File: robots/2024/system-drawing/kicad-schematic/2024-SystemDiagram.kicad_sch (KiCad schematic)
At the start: 207 parts

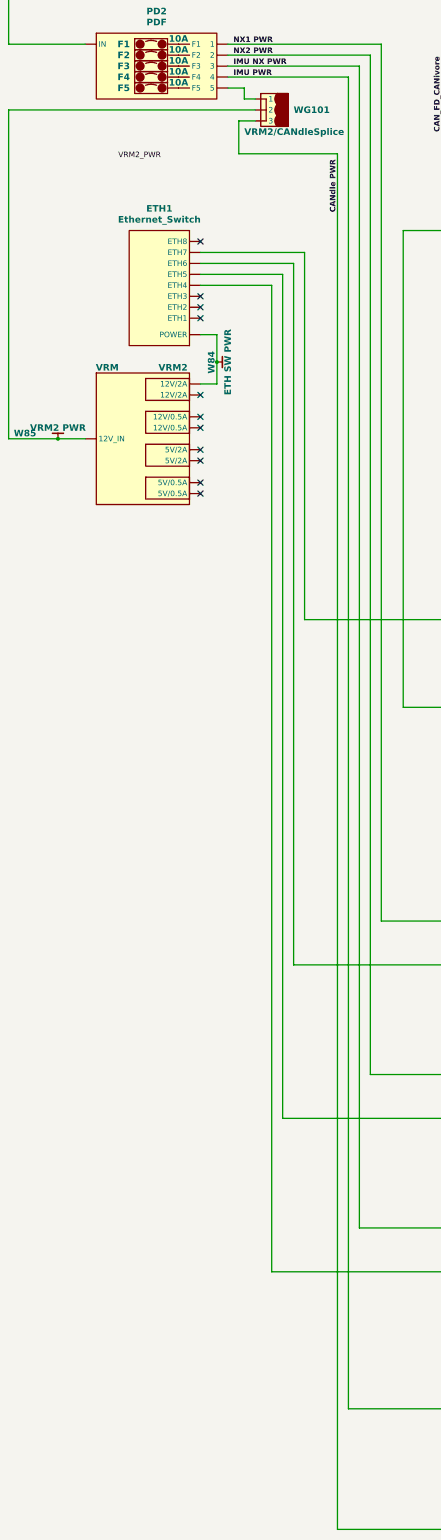
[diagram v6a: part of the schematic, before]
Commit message: Move Candle to VRM2 in sys dwg
Signed-off-by: Scott Berman <sgberman1@gmail.com>
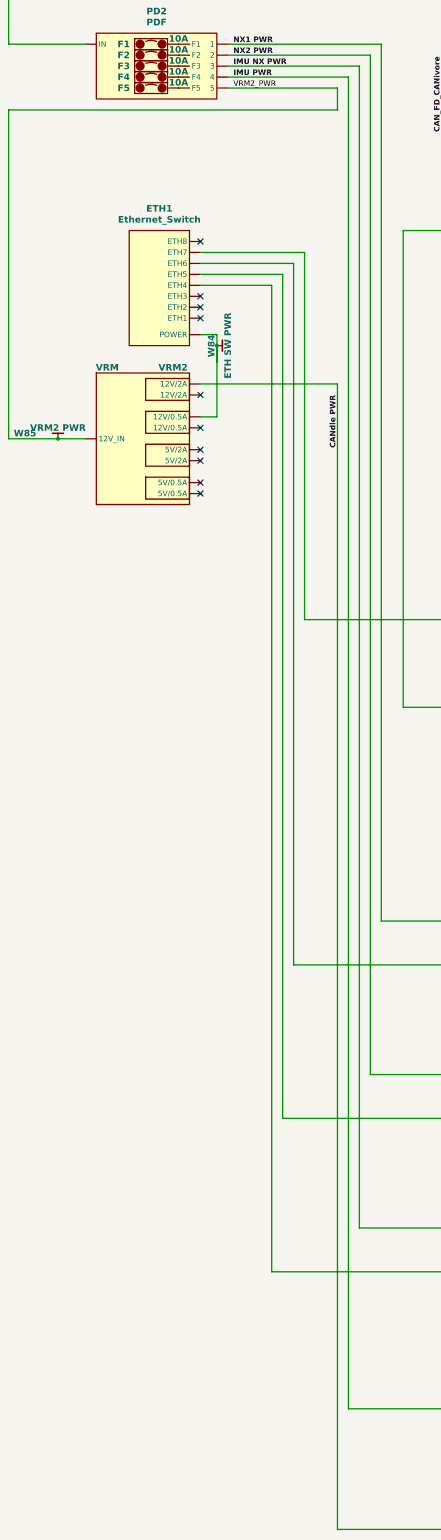
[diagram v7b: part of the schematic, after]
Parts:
- removed WG101: VRM2/CANdleSplice, symbol SystemDiagram:Wago_3
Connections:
- net CANdle PWR: now also VRM2. (5V/2A)
- net VRM2_PWR: now also PD2. (IN), VRM2. (5V/2A), W85.
- net at POE1. (RJ45S): now also RDO1. (POWER); no longer VRM1. (5V/2A)
- net at RDO1. (POWER): now also ETH1. (POWER); no longer VRM1. (5V/2A)
- net at ETH1. (POWER): now also NX1. (Power), W87.; no longer RDO1. (POWER)
- new net: VRM1. (5V/2A), W118., WG1. (4)
- new net: POE1. (RJ45S), VRM1. (5V/2A)
- new net: RDO1. (POWER), VRM1. (5V/2A)
- new net: CAN1. (USB), W67., WG1. (4)
- new net: ETH1. (POWER), NX2. (Power), W88.
- new net: MOT10. (PWR), MOT12. (PWR), W111.
- new net: ETH1. (POWER), VRM2. (5V/2A), W84.
- new net: ETH1. (POWER), NX3. (Power), W89.
- new net: MOT1. (PWR), MOT2. (PWR), W105.
- new net: MOT3. (PWR), MOT4. (PWR), W107.
- new net: IMU1. (RIO_PWM2), NX3. (Power), W47.
- no-connect marks 73 -> 72
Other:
- moved on the sheet: W84
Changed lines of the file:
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@@
   (junction (at 171.45 426.72) (diameter 0) (color 0 0 0 0)
   )
-  (junction (at 91.44 251.46) (diameter 0) (color 0 0 0 0)
-  )
   (junction (at 582.93 474.98) (diameter 0) (color 0 0 0 0)
   )
@@
   (junction (at 281.94 492.76) (diameter 0) (color 0 0 0 0)
   )
+  (junction (at 91.44 247.65) (diameter 0) (color 0 0 0 0)
+  )
   (junction (at 237.49 232.41) (diameter 0) (color 0 0 0 0)
   )
@@
   (no_connect (at 224.79 426.72))
   (no_connect (at 87.63 236.22))
-  (no_connect (at 87.63 264.16))
   (no_connect (at 220.98 259.08))
   (no_connect (at 191.77 469.9))
@@
     (stroke (width 0.254) (type default) (color 255 0 0 1))
   )
+  (wire (pts (xy 87.63 256.54) (xy 119.38 256.54))
+    (stroke (width 0.508) (type default) (color 255 0 0 1))
+  )
   (wire (pts (xy 487.68 326.39) (xy 436.88 326.39))
     (stroke (width 0.508) (type default) (color 255 0 0 1))
@@
     (stroke (width 0.254) (type default) (color 255 153 0 1))
   )
-  (wire (pts (xy 93.98 187.96) (xy 97.79 187.96))
-    (stroke (width 0.508) (type default) (color 255 0 0 1))
-  )
-  (wire (pts (xy 96.52 203.2) (xy 96.52 195.58))
+  (wire (pts (xy 93.98 187.96) (xy 119.38 187.96))
     (stroke (width 0.508) (type default) (color 255 0 0 1))
   )
@@
     (stroke (width 0.508) (type default) (color 255 0 0 1))
   )
-  (wire (pts (xy 96.52 195.58) (xy 100.33 195.58))
-    (stroke (width 0.508) (type default) (color 255 0 0 1))
-  )
-  (wire (pts (xy 87.63 256.54) (xy 91.44 256.54))
-    (stroke (width 0.254) (type default) (color 255 0 0 1))
-  )
   (wire (pts (xy 165.1 149.86) (xy 165.1 205.74))
     (stroke (width 0.508) (type default) (color 255 0 0 1))
@@
     (stroke (width 0.508) (type default) (color 255 0 0 1))
   )
-  (wire (pts (xy 91.44 245.11) (xy 91.44 251.46))
+  (wire (pts (xy 91.44 245.11) (xy 91.44 247.65))
     (stroke (width 0.254) (type default) (color 255 0 0 1))
   )
@@
     (stroke (width 0.508) (type default) (color 255 0 0 1))
   )
-  (wire (pts (xy 97.79 190.5) (xy 100.33 190.5))
-    (stroke (width 0.508) (type default) (color 255 0 0 1))
-  )
   (wire (pts (xy 73.025 64.77) (xy 92.71 64.77))
     (stroke (width 0.508) (type default) (color 255 0 0 1))
@@
     (stroke (width 0.508) (type default) (color 255 0 0 1))
   )
-  (wire (pts (xy 119.38 203.2) (xy 96.52 203.2))
-    (stroke (width 0.508) (type default) (color 255 0 0 1))
-  )
   (wire (pts (xy 580.39 400.05) (xy 595.63 400.05))
     (stroke (width 0) (type default))
@@
     (stroke (width 0.508) (type default) (color 255 0 0 1))
   )
-  (wire (pts (xy 119.38 203.2) (xy 119.38 521.97))
-    (stroke (width 0.508) (type default) (color 255 0 0 1))
-  )
   (wire (pts (xy 487.68 341.63) (xy 552.45 341.63))
     (stroke (width 0.254) (type default) (color 194 0 194 1))
@@
     (stroke (width 0.508) (type default) (color 255 0 0 1))
   )
+  (wire (pts (xy 91.44 247.65) (xy 91.44 251.46))
+    (stroke (width 0) (type default))
+  )
   (wire (pts (xy 601.98 331.47) (xy 607.06 331.47))
     (stroke (width 0.254) (type default) (color 255 153 0 1))
@@
     (stroke (width 0.254) (type default) (color 194 0 194 1))
   )
-  (wire (pts (xy 97.79 187.96) (xy 97.79 190.5))
+  (wire (pts (xy 119.38 187.96) (xy 119.38 193.04))
     (stroke (width 0.508) (type default) (color 255 0 0 1))
   )
@@
     (stroke (width 0.254) (type default) (color 255 153 0 1))
   )
+  (wire (pts (xy 91.44 264.16) (xy 87.63 264.16))
+    (stroke (width 0.254) (type default) (color 255 0 0 1))
+  )
   (wire (pts (xy 401.32 194.31) (xy 401.32 368.3))
     (stroke (width 0.254) (type default) (color 194 0 194 1))
   )
-  (wire (pts (xy 91.44 251.46) (xy 91.44 256.54))
+  (wire (pts (xy 91.44 247.65) (xy 91.44 264.16))
     (stroke (width 0.254) (type default) (color 255 0 0 1))
   )
@@
     (stroke (width 0.508) (type default) (color 255 0 0 1))
   )
+  (wire (pts (xy 119.38 256.54) (xy 119.38 521.97))
+    (stroke (width 0.508) (type default) (color 255 0 0 1))
+  )
   (wire (pts (xy 534.67 144.78) (xy 510.54 144.78))
     (stroke (width 0.254) (type default) (color 194 0 194 1))
@@
     (stroke (width 0.254) (type default) (color 194 0 194 1))
   )
-  (wire (pts (xy 43.18 193.04) (xy 100.33 193.04))
+  (wire (pts (xy 43.18 193.04) (xy 119.38 193.04))
     (stroke (width 0.508) (type default) (color 255 0 0 1))
   )
@@
     (effects (font (face "FreeSans") (size 1.27 1.27) bold) (justify left bottom))
   )
-  (label "CANdle PWR" (at 119.38 204.47 270) (fields_autoplaced)
+  (label "CANdle PWR" (at 119.38 259.08 270) (fields_autoplaced)
     (effects (font (face "FreeSans") (size 1.27 1.27) bold) (justify right bottom))
   )
-  (label "VRM2_PWR" (at 68.58 204.47 0) (fields_autoplaced)
-    (effects (font (size 1.27 1.27)) (justify left bottom))
-  )
   (label "CAN_CLIMBER_TO_INTAKE" (at 591.82 391.16 180) (fields_autoplaced)
     (effects (font (face "FreeSans") (size 1.27 1.27) (thickness 0.254) bold) (justify right bottom))
@@
     (effects (font (face "FreeSans") (size 1.27 1.27) bold) (justify right bottom))
   )
+  (label "VRM2_PWR" (at 95.25 187.96 0) (fields_autoplaced)
+    (effects (font (size 1.27 1.27)) (justify left bottom))
+  )
   (label "DUMP BB PWR" (at 529.59 439.42 180) (fields_autoplaced)
     (effects (font (face "FreeSans") (size 1.27 1.27) bold) (justify right bottom))
@@
     )
   )
-  (symbol (lib_id "SystemDiagram:WireTag") (at 91.44 251.46 270) (unit 1)
+  (symbol (lib_id "SystemDiagram:WireTag") (at 91.44 247.65 270) (unit 1)
     (in_bom yes) (on_board yes) (dnp no)
-    (property "Reference" "W84" (at 90.17 248.92 0)
+    (property "Reference" "W84" (at 90.17 245.11 0)
       (effects (font (face "FreeSans") (size 1.524 1.524) bold) (justify left))
     )
-    (property "Value" "ETH SW PWR" (at 93.98 251.46 0)
+    (property "Value" "ETH SW PWR" (at 93.98 247.65 0)
       (effects (font (face "FreeSans") (size 1.524 1.524) bold))
     )
-    (property "Footprint" "" (at 91.44 251.46 0)
+    (property "Footprint" "" (at 91.44 247.65 0)
       (effects (font (size 1.27 1.27)) hide)
     )
-    (property "Datasheet" "" (at 91.44 251.46 0)
+    (property "Datasheet" "" (at 91.44 247.65 0)
       (effects (font (size 1.27 1.27)) hide)
     )
@@
         )
       )
-    )
-  )
-  (symbol (lib_id "SystemDiagram:Wago_3") (at 102.87 193.04 0) (unit 1)
-    (in_bom yes) (on_board yes) (dnp no)
-    (property "Reference" "WG101" (at 109.22 193.04 0)
-      (effects (font (face "FreeSans") (size 1.524 1.524) bold) (justify left))
-    )
-    (property "Value" "VRM2/CANdleSplice" (at 97.79 198.12 0)
-      (effects (font (face "FreeSans") (size 1.524 1.524) bold) (justify left))
-    )
-    (property "Footprint" "" (at 102.87 193.04 0)
-      (effects (font (size 1.27 1.27)) hide)
-    )
-    (property "Datasheet" "" (at 102.87 193.04 0)
-      (effects (font (size 1.27 1.27)) hide)
-    )
-    (pin "")
-    (pin "")
-    (pin "")
-    (instances
-      (project "2024-SystemDiagram"
-        (path "/12a52703-e3f4-4774-b510-3055ab1abf35"
-          (reference "WG101") (unit 1)
-        )
-      )

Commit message: Sys dwg: Swap right and left robot, move alt and catapult motors to FD
Signed-off-by: Scott Berman <sgberman1@gmail.com>
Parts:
- removed CAN4: CAN_Terminator, symbol SystemDiagram:CAN_Terminator
- removed W51: CATAPULT2 PWM, symbol SystemDiagram:WireTag
- removed WJ104: ~, symbol SystemDiagram:Wire_Junction
- added CAN102: CAN_Terminator, symbol SystemDiagram:CAN_Terminator
- added W133: CAN, symbol SystemDiagram:WireTag
- ENC1: value Left Shaft_Encoder -> Right Shaft_Encoder
- ENC2: value Right Shaft_Encoder -> Left Shaft_Encoder
- MOT1: value Kraken Left Front Drive Motor -> Kraken Right Back Drive Motor; CAN ID FD ID 4 -> FD ID 1
- MOT2: value Kraken Left Back Drive Motor -> Kraken Right Front Drive Motor; CAN ID FD ID 5 -> FD ID 2
- MOT3: value Kraken Right Front Drive Motor -> Kraken Left Back Drive Motor; CAN ID FD ID 2 -> FD ID 5
- MOT4: value Kraken Right Back Drive Motor -> Kraken Left Front Drive Motor; CAN ID FD ID 1 -> FD ID 4
- MOT5: CAN ID (none) -> FD ID 14
- MOT6: CAN ID (none) -> FD ID 15
- MOT7: CAN ID CAN ID 9 -> FD ID 9
- NX1: value NX1 -> NX1-LEFT
- NX2: value NX2 -> NX2-RIGHT
- W122: value CATAPULT1 PWM -> CAN
- W124: value CATAPULT2 PWM -> CAN
- W22: value Left Shaft Encoder -> Right Shaft Encoder
- W23: value Right Shaft Encoder -> Left Shaft Encoder
- W4: value LEFT FRONT DRIVE PWR -> RIGHT BACK DRIVE PWR
- W5: value LEFT BACK DRIVE PWR -> RIHGT FRONT DRIVE PWR
- W6: value RIGHT FRONT DRIVE PWR -> LEFT_BACK_DRIVE PWR
- W7: value RIGHT BACK DRIVE PWR -> LEFT FRONT DRIVE PWR
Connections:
- net CLIMBER ENC POT RIO: now also RIO1.ENC_AD4; no longer RIO1.ENC_AD5
- net LEFT BACK DRIVE PWR: now also MOT3. (PWR), PD1.T14, W6.; no longer MOT2. (PWR), PD1.T1, W5.
- net LEFT ENC: now also ENC2. (OUT), RIO1.DIO8, RIO1.DIO9, W23.; no longer ENC1. (OUT), RIO1.DIO6, RIO1.DIO7, W22.
- net LEFT FRONT DRIVE PWR: now also MOT4. (PWR), PD1.T15, W7.; no longer MOT1. (PWR), PD1.T0, W4.
- net RIGHT BACK DRIVE PWR: now also MOT1. (PWR), PD1.T0, W4.; no longer MOT4. (PWR), PD1.T15, W7.
- net RIGHT ENC: now also ENC1. (OUT), RIO1.DIO6, RIO1.DIO7, W22.; no longer ENC2. (OUT), RIO1.DIO8, RIO1.DIO9, W23.
- net RIGHT FRONT DRIVE PWR: now also MOT2. (PWR), PD1.T1, W5.; no longer MOT3. (PWR), PD1.T14, W6.
- net TRAP EXTEND ENC POT RIO: now also RIO1.ENC_AD5; no longer RIO1.ENC_AD4
- net at POE1. (RJ45S): now also RDO1. (POWER); no longer VRM1. (5V/2A)
- net at RDO1. (POWER): now also ETH1. (POWER); no longer VRM1. (5V/2A)
- net at ETH1. (POWER): now also NX1. (Power), W87.; no longer RDO1. (POWER)
- net CAN_FD_INTAKE_PIVOT_TO_ALT: now reaches MOT14. (PWR), W110.
- net CAN_FD_INTAKE_PIVOT_TO_ALT: now also MOT7. (PWR), W117., W129., WJ108.1 (J)
- removed net CAN_ALT_TO_XFER_ROLLERS: MOT10. (PWR), MOT7. (PWR), W117., W129., WJ108.1 (J)
- removed net CAN_FD_LEFT_BACK_INTAKE_PIVOT: MOT14. (PWR), MOT2. (PWR), W106.
- removed net CAN_FD_TURRET_LEFT_FRONT: MOT1. (PWR), MOT8. (PWR), W119.
- removed net CAN_HOLD_TO_ALT: MOT15. (PWR), MOT7. (PWR), W127.
- removed net CATAPULT1 PWM: MOT5. (PWR), RIO1.PWM0, W122., W50., WJ102.1 (J)
- removed net CATAPULT2 PWM: MOT6. (PWR), RIO1.PWM1, W124.
- new net: CAN102., MOT6. (PWR), W133.
- new net: VRM1. (5V/2A), W118., WG1. (4)
- new net: POE1. (RJ45S), VRM1. (5V/2A)
- new net: RDO1. (POWER), VRM1. (5V/2A)
- new net: CAN1. (USB), W67., WG1. (4)
- new net: ETH1. (POWER), NX2. (Power), W88.
- new net: MOT10. (PWR), MOT12. (PWR), W111.
- new net: ETH1. (POWER), VRM2. (5V/2A), W84.
- new net: ETH1. (POWER), NX3. (Power), W89.
- new net: MOT1. (PWR), MOT2. (PWR), W105.
- new net: MOT3. (PWR), MOT4. (PWR), W107.
- new net: MOT5. (PWR), MOT6. (PWR), W124.
- new net: IMU1. (RIO_PWM2), NX3. (Power), W47.
- new net CAN_FD_ALT_TO_CATAPULT1: MOT5. (PWR), MOT7. (PWR), W122.
- new net CAN_FD_RIGHT_FRONT_INTAKE_PIVOT: MOT14. (PWR), MOT2. (PWR), W106.
- new net CAN_FD_TURRET_RIGHT_BACK: MOT1. (PWR), MOT8. (PWR), W119.
- new net CAN_HOLD_TO_TRANSFER: MOT10. (PWR), MOT15. (PWR), W127.
